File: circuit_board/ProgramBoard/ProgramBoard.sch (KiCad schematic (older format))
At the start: 3 parts, among them P1 CONN5X2, P2 TC2030_IDC, P3 TC2030_IDC

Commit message: examined the program board
try to switch to 10 pin tag cable to combine the programmer, UART, and power.
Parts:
- removed P2, P3: TC2030_IDC, SensorDemo_pcb:HEADER_3X2, symbol SensorDemo_connector:TC2030_IDC
- added P2: HEADER_6, SensorDemo_pcb:HEADER_6, symbol SensorDemo_connector:HEADER_6
- added U1: SparkFun_FT231X_Breakout, SensorDemo_pcb:SparkFun_FT231X_Breakout, symbol SensorDemo_discrete:SparkFun_FT231X_Breakout
- P1: value CONN5X2 -> IDC-10; footprint SensorDemo_pcb:FT231X_breakout -> SensorDemo_pcb:IDC_10
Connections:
- net labels removed: +5V, GND, PGC, PGD, PGM, RX, TX, VDD, VSS, ~MCLR
- wire segments 22 -> 0
- no-connect marks 6 -> 0
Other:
- note added: "IDC-10 connector"
- note added: "PICkit 3 connector"
- note removed: "From the USB, PIN 6 on top (in pic in ref)"
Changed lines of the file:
@@
 $EndDescr
 $Comp
-L SensorDemo_connector:TC2030_IDC P2
-U 1 1 6049E1C8
-P 2900 1700
-F 0 "P2" H 2900 1973 50  0000 C CNN
-F 1 "TC2030_IDC" H 2900 1250 50  0001 C CNN
-F 2 "SensorDemo_pcb:HEADER_3X2" H 6200 -450 60  0001 C CNN
-F 3 "" H 6200 -450 60  0000 C CNN
-	1    2900 1700
+L SensorDemo_discrete:SparkFun_FT231X_Breakout U1
+U 1 1 603DD946
+P 6800 3500
+F 0 "U1" H 6800 4187 60  0000 C CNN
+F 1 "SparkFun_FT231X_Breakout" H 6800 4081 60  0000 C CNN
+F 2 "SensorDemo_pcb:SparkFun_FT231X_Breakout" H 6800 3650 60  0001 C CNN
+F 3 "https://www.tag-connect.com/product/tc2050-idc-nl-10-pin-no-legs-cable-with-ribbon-connector" H 6800 3650 60  0001 C CNN
+	1    6800 3500
+	1    0    0    -1
+$EndComp
+Text Notes 6950 4650 0    50   ~ 0
+PICkit 3 connector
+$Comp
+L SensorDemo_connector:HEADER_6 P2
+U 1 1 603DF1C0
+P 7250 4800
+F 0 "P2" H 7588 4692 50  0000 L CNN
+F 1 "HEADER_6" H 7250 4250 50  0001 C CNN
+F 2 "SensorDemo_pcb:HEADER_6" H 10550 2600 60  0001 C CNN
+F 3 "" H 10550 2600 60  0000 C CNN
+	1    7250 4800
 	1    0    0    -1
 $EndComp
 $Comp
-L SensorDemo_connector:TC2030_IDC P3
-U 1 1 6049EA08
-P 2950 2800
-F 0 "P3" H 2950 3073 50  0000 C CNN
-F 1 "TC2030_IDC" H 2950 2350 50  0001 C CNN
-F 2 "SensorDemo_pcb:HEADER_3X2" H 6250 650 60  0001 C CNN
-F 3 "" H 6250 650 60  0000 C CNN
-	1    2950 2800
+L SensorDemo_connector:CONN5X2 P1
+U 1 1 603DFAE2
+P 5000 4850
+F 0 "P1" H 5000 5337 60  0000 C CNN
+F 1 "IDC-10" H 5000 5231 60  0000 C CNN
+F 2 "SensorDemo_pcb:IDC_10" H 8300 2700 60  0001 C CNN
+F 3 "" H 8300 2700 60  0000 C CNN
+	1    5000 4850
 	1    0    0    -1
 $EndComp
-Wire Wire Line
-	1900 1350 1900 1500
-Wire Wire Line
-	1900 1500 1800 1500
-$Comp
-L SensorDemo_power_supply:+5V #PS01
-U 1 1 604A19ED
-P 1900 1350
-F 0 "#PS01" H 1900 1300 50  0001 C CNN
-F 1 "+5V" H 1968 1378 50  0000 L CNN
-F 2 "" H 1905 1045 50  0001 C CNN
-F 3 "" H 1905 1045 50  0001 C CNN
-	1    1900 1350
-	1    0    0    -1
-$EndComp
-Wire Wire Line
-	2550 1800 2500 1800
-Wire Wire Line
-	2500 2000 3300 2000
-Wire Wire Line
-	3300 2000 3300 1800
-Wire Wire Line
-	3300 1800 3250 1800
-Wire Wire Line
-	2500 1800 2500 2000
-Wire Wire Line
-	2500 2050 2500 2000
-Connection ~ 2500 2000
-$Comp
-L SensorDemo_power_supply:+5V #PS03
-U 1 1 604A80D9
-P 2500 2050
-F 0 "#PS03" H 2500 2000 50  0001 C CNN
-F 1 "+5V" H 2432 2077 50  0000 R CNN
-F 2 "" H 2505 1745 50  0001 C CNN
-F 3 "" H 2505 1745 50  0001 C CNN
-	1    2500 2050
-	-1   0    0    1
-$EndComp
-Wire Wire Line
-	3250 1700 3300 1700
-Wire Wire Line
-	3300 1700 3300 1600
-Wire Wire Line
-	3300 1600 3250 1600
-Wire Wire Line
-	3300 1400 3300 1600
-Connection ~ 3300 1600
-$Comp
-L SensorDemo_power_supply:GND #PS04
-U 1 1 604A954E
-P 3300 1350
-F 0 "#PS04" H 3300 1225 50  0001 C CNN
-F 1 "GND" H 3300 1275 50  0001 C CNN
-F 2 "" H 3300 1350 50  0001 C CNN
-F 3 "" H 3300 1350 50  0001 C CNN
-	1    3300 1350
-	-1   0    0    1
-$EndComp
-Wire Wire Line
-	3550 2700 3300 2700
-Wire Wire Line
-	3550 2800 3300 2800
-Wire Wire Line
-	3550 2900 3300 2900
-Wire Wire Line
-	2350 2700 2600 2700
-Wire Wire Line
-	2350 2800 2600 2800
-Wire Wire Line
-	2350 2900 2600 2900
-Text Label 3550 2700 2    50   ~ 0
-~MCLR
-Text Label 3550 2800 2    50   ~ 0
-VSS
-Text Label 3550 2900 2    50   ~ 0
-PGC
-Text Label 2350 2700 0    50   ~ 0
-VDD
-Text Label 2350 2800 0    50   ~ 0
-PGD
-Text Label 2350 2900 0    50   ~ 0
-PGM
-Text Notes 1250 1100 0    50   ~ 0
-From the USB, PIN 6 on top (in pic in ref)
-$Comp
-L SensorDemo_connector:CONN5X2 P1
-U 1 1 604B47DD
-P 1450 1700
-F 0 "P1" H 1450 2187 60  0000 C CNN
-F 1 "CONN5X2" H 1450 2081 60  0000 C CNN
-F 2 "SensorDemo_pcb:FT231X_breakout" H 4750 -450 60  0000 C CNN
-F 3 "" H 4750 -450 60  0000 C CNN
-	1    1450 1700
-	1    0    0    -1
-$EndComp
-Wire Wire Line
-	900  1900 1100 1900
-Text Label 900  1900 0    50   ~ 0
-RX
-Wire Wire Line
-	2000 1900 1800 1900
-Text Label 2000 1900 2    50   ~ 0
-TX
-Wire Wire Line
-	1050 2050 1050 1500
-Wire Wire Line
-	1050 1500 1100 1500
-$Comp
-L SensorDemo_power_supply:GND #PS0101
-U 1 1 604BC56C
-P 1050 2100
-F 0 "#PS0101" H 1050 1975 50  0001 C CNN
-F 1 "GND" H 1050 2025 50  0001 C CNN
-F 2 "" H 1050 2100 50  0001 C CNN
-F 3 "" H 1050 2100 50  0001 C CNN
-	1    1050 2100
-	1    0    0    -1
-$EndComp
-NoConn ~ 1100 1600
-NoConn ~ 1100 1700
-NoConn ~ 1100 1800
-NoConn ~ 1800 1800
-NoConn ~ 1800 1700
-NoConn ~ 1800 1600
+Text Notes 4650 5350 0    50   ~ 0
+IDC-10 connector
 $EndSCHEMATC

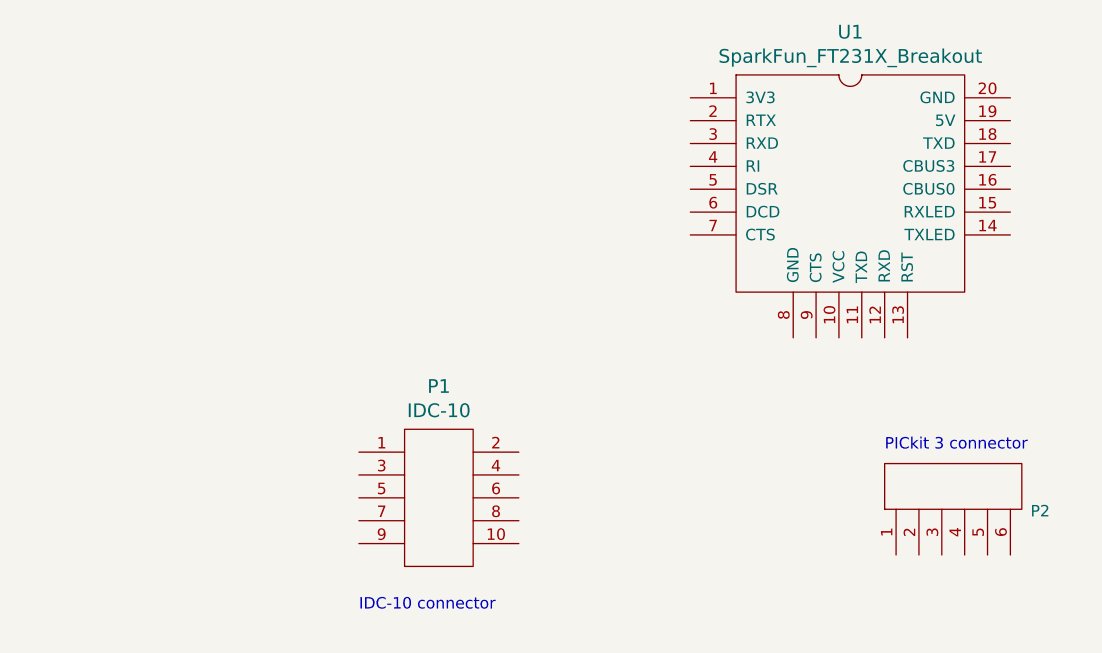
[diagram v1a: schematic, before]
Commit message: SensorDemo and Program board modified
1. SensorDemo board minor adjustment, 3D models added.
2. the TC2050 cable is added and routed on programmer board.
3. 3D models are added into the library.
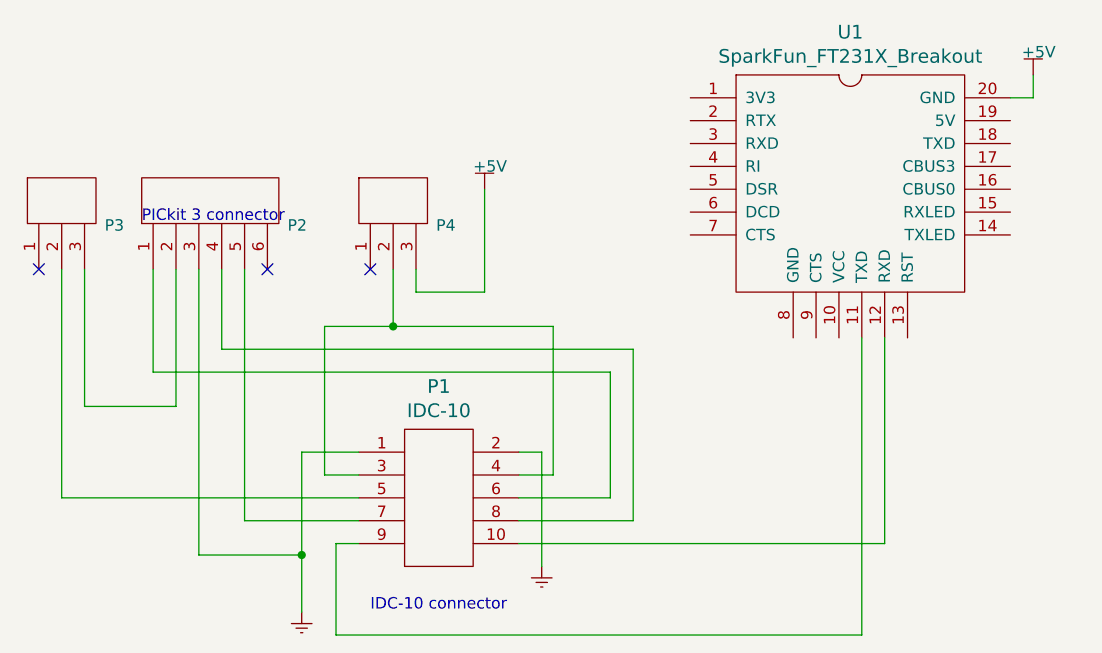
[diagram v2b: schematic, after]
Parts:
- added P3, P4: HEADER_3, SensorDemo_pcb:HEADER_3, symbol SensorDemo_connector:HEADER_3
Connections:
- net at U1.11 (TXD): now also P1.9
- net at U1.12 (RXD): now also P1.10
- net at P2.1: now also P1.6
- net at P2.2: now also P3.3
- net at P2.3: now also P1.1
- net at P2.4: now also P1.8
- net at P2.5: now also P1.7
- net at P1.3: now also P1.4, P4.2
- net at P1.5: now also P3.2
- no-connect marks 0 -> 3
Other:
- moved on the sheet: P2
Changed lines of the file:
@@
 	1    0    0    -1
 $EndComp
-Text Notes 6950 4650 0    50   ~ 0
+Text Notes 3700 3650 0    50   ~ 0
 PICkit 3 connector
 $Comp
 L SensorDemo_connector:HEADER_6 P2
 U 1 1 603DF1C0
-P 7250 4800
-F 0 "P2" H 7588 4692 50  0000 L CNN
-F 1 "HEADER_6" H 7250 4250 50  0001 C CNN
-F 2 "SensorDemo_pcb:HEADER_6" H 10550 2600 60  0001 C CNN
-F 3 "" H 10550 2600 60  0000 C CNN
-	1    7250 4800
+P 4000 3550
+F 0 "P2" H 4338 3442 50  0000 L CNN
+F 1 "HEADER_6" H 4000 3000 50  0001 C CNN
+F 2 "SensorDemo_pcb:HEADER_6" H 7300 1350 60  0001 C CNN
+F 3 "" H 7300 1350 60  0000 C CNN
+	1    4000 3550
 	1    0    0    -1
 $EndComp
@@
 	1    0    0    -1
 $EndComp
-Text Notes 4650 5350 0    50   ~ 0
+Text Notes 4700 5350 0    50   ~ 0
 IDC-10 connector
+$Comp
+L SensorDemo_power_supply:GND #PS03
+U 1 1 603D34E0
+P 5450 5200
+F 0 "#PS03" H 5450 5075 50  0001 C CNN
+F 1 "GND" H 5450 5125 50  0001 C CNN
+F 2 "" H 5450 5200 50  0001 C CNN
+F 3 "" H 5450 5200 50  0001 C CNN
+	1    5450 5200
+	1    0    0    -1
+$EndComp
+$Comp
+L SensorDemo_power_supply:+5V #PS01
+U 1 1 603D79A0
+P 7600 3000
+F 0 "#PS01" H 7600 2950 50  0001 C CNN
+F 1 "+5V" H 7550 3100 50  0000 L CNN
+F 2 "" H 7605 2695 50  0001 C CNN
+F 3 "" H 7605 2695 50  0001 C CNN
+	1    7600 3000
+	1    0    0    -1
+$EndComp
+Wire Wire Line
+	7600 3000 7600 3100
+Wire Wire Line
+	7600 3100 7500 3100
+Wire Wire Line
+	5350 4650 5450 4650
+Wire Wire Line
+	5450 4650 5450 5150
+Wire Wire Line
+	5350 4750 5500 4750
+Wire Wire Line
+	5500 4750 5500 4100
+Wire Wire Line
+	4500 4750 4500 4100
+Wire Wire Line
+	4500 4750 4650 4750
+Wire Wire Line
+	4650 4650 4400 4650
+Wire Wire Line
+	4400 4650 4400 5100
+$Comp
+L SensorDemo_power_supply:GND #PS04
+U 1 1 603DAB05
+P 4400 5400
+F 0 "#PS04" H 4400 5275 50  0001 C CNN
+F 1 "GND" H 4400 5325 50  0001 C CNN
+F 2 "" H 4400 5400 50  0001 C CNN
+F 3 "" H 4400 5400 50  0001 C CNN
+	1    4400 5400
+	1    0    0    -1
+$EndComp
+Wire Wire Line
+	3850 3850 3850 4450
+Wire Wire Line
+	3750 3850 3750 4300
+Wire Wire Line
+	3750 4300 5750 4300
+Wire Wire Line
+	5750 4300 5750 4850
+Wire Wire Line
+	5750 4850 5350 4850
+Wire Wire Line
+	3950 3850 3950 5100
+Wire Wire Line
+	3950 5100 4400 5100
+Connection ~ 4400 5100
+Wire Wire Line
+	4400 5100 4400 5350
+Wire Wire Line
+	4050 3850 4050 4200
+Wire Wire Line
+	4050 4200 5850 4200
+Wire Wire Line
+	5850 4200 5850 4950
+Wire Wire Line
+	5850 4950 5350 4950
+Wire Wire Line
+	4150 3850 4150 4950
+Wire Wire Line
+	4150 4950 4650 4950
+NoConn ~ 4250 3850
+Wire Wire Line
+	4650 5050 4550 5050
+Wire Wire Line
+	4550 5050 4550 5450
+Wire Wire Line
+	4550 5450 6850 5450
+Wire Wire Line
+	6850 5450 6850 4150
+Wire Wire Line
+	6950 4150 6950 5050
+Wire Wire Line
+	6950 5050 5350 5050
+Wire Wire Line
+	5500 4100 4800 4100
+$Comp
+L SensorDemo_connector:HEADER_3 P4
+U 1 1 603E9635
+P 4800 3550
+F 0 "P4" H 4988 3442 50  0000 L CNN
+F 1 "HEADER_3" H 4800 3000 50  0001 C CNN
+F 2 "SensorDemo_pcb:HEADER_3" H 8100 1350 60  0001 C CNN
+F 3 "" H 8100 1350 60  0000 C CNN
+	1    4800 3550
+	1    0    0    -1
+$EndComp
+$Comp
+L SensorDemo_power_supply:+5V #PS02
+U 1 1 603EB14F
+P 5200 3500
+F 0 "#PS02" H 5200 3450 50  0001 C CNN
+F 1 "+5V" H 5150 3600 50  0000 L CNN
+F 2 "" H 5205 3195 50  0001 C CNN
+F 3 "" H 5205 3195 50  0001 C CNN
+	1    5200 3500
+	1    0    0    -1
+$EndComp
+Wire Wire Line
+	5200 3500 5200 3950
+Wire Wire Line
+	4900 3850 4900 3950
+Wire Wire Line
+	4900 3950 5200 3950
+NoConn ~ 4700 3850
+Wire Wire Line
+	4800 3850 4800 4100
+Connection ~ 4800 4100
+Wire Wire Line
+	4800 4100 4500 4100
+$Comp
+L SensorDemo_connector:HEADER_3 P3
+U 1 1 603EEBCF
+P 3350 3550
+F 0 "P3" H 3538 3442 50  0000 L CNN
+F 1 "HEADER_3" H 3350 3000 50  0001 C CNN
+F 2 "SensorDemo_pcb:HEADER_3" H 6650 1350 60  0001 C CNN
+F 3 "" H 6650 1350 60  0000 C CNN
+	1    3350 3550
+	1    0    0    -1
+$EndComp
+Wire Wire Line
+	3450 3850 3450 4450
+NoConn ~ 3250 3850
+Wire Wire Line
+	3350 3850 3350 4850
+Wire Wire Line
+	3850 4450 3450 4450
+Wire Wire Line
+	4650 4850 3350 4850
 $EndSCHEMATC

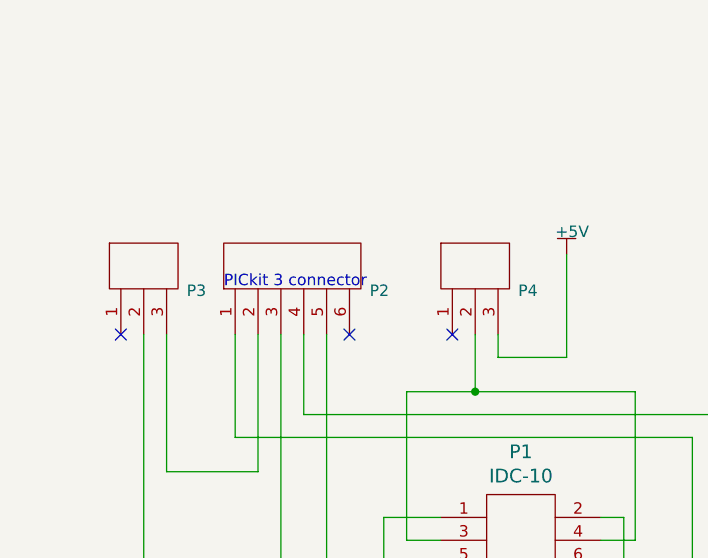
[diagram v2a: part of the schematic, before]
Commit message: updated SensoDemo and ProgramBoard
INA126 is replaced by INA333.
TC2050-IDC-NL cable will be used for powering and programming.
both boards should be done.
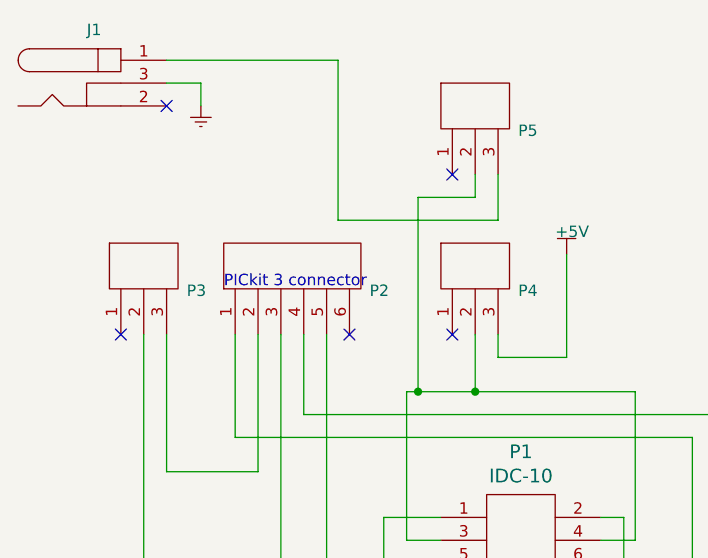
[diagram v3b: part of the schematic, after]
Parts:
- added J1: BARREL_JACK, SensorDemo_pcb:BARREL_JACK, symbol SensorDemo_connector:BARREL_JACK
- added P5: HEADER_3, SensorDemo_pcb:HEADER_3, symbol SensorDemo_connector:HEADER_3
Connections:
- net at P1.3, P1.4, P4.2: now also P5.2
- new net: J1.1, P5.3
- no-connect marks 3 -> 5
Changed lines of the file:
@@
 Connection ~ 4800 4100
 Wire Wire Line
-	4800 4100 4500 4100
+	4800 4100 4550 4100
 $Comp
 L SensorDemo_connector:HEADER_3 P3
@@
 Wire Wire Line
 	4650 4850 3350 4850
+$Comp
+L SensorDemo_connector:BARREL_JACK J1
+U 1 1 6047A3B5
+P 3150 2750
+F 0 "J1" H 3133 2983 50  0000 C CNN
+F 1 "BARREL_JACK" H 3150 2550 50  0001 C CNN
+F 2 "SensorDemo_pcb:BARREL_JACK" H 3150 2750 60  0001 C CNN
+F 3 "" H 3150 2750 60  0000 C CNN
+	1    3150 2750
+	1    0    0    -1
+$EndComp
+$Comp
+L SensorDemo_connector:HEADER_3 P5
+U 1 1 6047EE8D
+P 4800 2850
+F 0 "P5" H 4988 2742 50  0000 L CNN
+F 1 "HEADER_3" H 4800 2300 50  0001 C CNN
+F 2 "SensorDemo_pcb:HEADER_3" H 8100 650 60  0001 C CNN
+F 3 "" H 8100 650 60  0000 C CNN
+	1    4800 2850
+	1    0    0    -1
+$EndComp
+NoConn ~ 4700 3150
+Wire Wire Line
+	4800 3150 4800 3250
+Wire Wire Line
+	4800 3250 4550 3250
+Wire Wire Line
+	4550 3250 4550 4100
+Connection ~ 4550 4100
+Wire Wire Line
+	4550 4100 4500 4100
+Wire Wire Line
+	4900 3150 4900 3350
+Wire Wire Line
+	4900 3350 4200 3350
+Wire Wire Line
+	4200 3350 4200 2650
+Wire Wire Line
+	3450 2650 4200 2650
+$Comp
+L SensorDemo_power_supply:GND #PS?
+U 1 1 6048CCC2
+P 3600 2900
+F 0 "#PS?" H 3600 2775 50  0001 C CNN
+F 1 "GND" H 3600 2825 50  0001 C CNN
+F 2 "" H 3600 2900 50  0001 C CNN
+F 3 "" H 3600 2900 50  0001 C CNN
+	1    3600 2900
+	1    0    0    -1
+$EndComp
+Wire Wire Line
+	3600 2850 3600 2750
+Wire Wire Line
+	3600 2750 3450 2750
+NoConn ~ 3450 2850
 $EndSCHEMATC

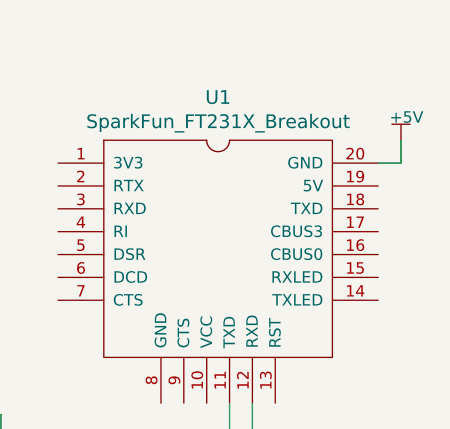
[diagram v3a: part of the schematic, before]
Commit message: updated schematic
-fixed programming board 5v
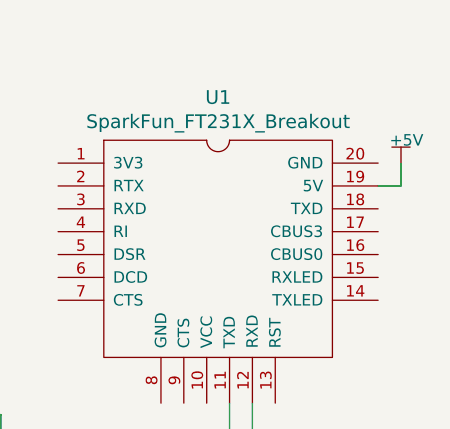
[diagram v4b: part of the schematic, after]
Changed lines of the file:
@@
 L SensorDemo_power_supply:+5V #PS01
 U 1 1 603D79A0
-P 7600 3000
-F 0 "#PS01" H 7600 2950 50  0001 C CNN
-F 1 "+5V" H 7550 3100 50  0000 L CNN
-F 2 "" H 7605 2695 50  0001 C CNN
-F 3 "" H 7605 2695 50  0001 C CNN
-	1    7600 3000
+P 7600 3100
+F 0 "#PS01" H 7600 3050 50  0001 C CNN
+F 1 "+5V" H 7550 3200 50  0000 L CNN
+F 2 "" H 7605 2795 50  0001 C CNN
+F 3 "" H 7605 2795 50  0001 C CNN
+	1    7600 3100
 	1    0    0    -1
 $EndComp
 Wire Wire Line
-	7600 3000 7600 3100
+	7600 3100 7600 3200
 Wire Wire Line
-	7600 3100 7500 3100
+	7600 3200 7500 3200
 Wire Wire Line
 	5350 4650 5450 4650

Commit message: Revert "Revert "Merge branch 'master' of https://github.com/zrs5532/mri_demo""
This reverts commit c7bcd66b67d9c03c78e75f611b5453059c538dec.
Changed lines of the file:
@@
 L SensorDemo_power_supply:+5V #PS01
 U 1 1 603D79A0
-P 7600 3100
-F 0 "#PS01" H 7600 3050 50  0001 C CNN
-F 1 "+5V" H 7550 3200 50  0000 L CNN
-F 2 "" H 7605 2795 50  0001 C CNN
-F 3 "" H 7605 2795 50  0001 C CNN
-	1    7600 3100
-	1    0    0    -1
-$EndComp
-Wire Wire Line
-	7600 3100 7600 3200
-Wire Wire Line
-	7600 3200 7500 3200
+P 7750 3100
+F 0 "#PS01" H 7750 3050 50  0001 C CNN
+F 1 "+5V" H 7700 3200 50  0000 L CNN
+F 2 "" H 7755 2795 50  0001 C CNN
+F 3 "" H 7755 2795 50  0001 C CNN
+	1    7750 3100
+	1    0    0    -1
+$EndComp
+Wire Wire Line
+	7750 3100 7750 3200
+Wire Wire Line
+	7750 3200 7500 3200
 Wire Wire Line
 	5350 4650 5450 4650
@@
 	4650 4850 3350 4850
 $Comp
+L SensorDemo_connector:HEADER_3 P5
+U 1 1 6047EE8D
+P 4800 2850
+F 0 "P5" H 4988 2742 50  0000 L CNN
+F 1 "HEADER_3" H 4800 2300 50  0001 C CNN
+F 2 "SensorDemo_pcb:HEADER_3" H 8100 650 60  0001 C CNN
+F 3 "" H 8100 650 60  0000 C CNN
+	1    4800 2850
+	1    0    0    -1
+$EndComp
+NoConn ~ 4700 3150
+Wire Wire Line
+	4800 3150 4800 3250
+Wire Wire Line
+	4800 3250 4550 3250
+Wire Wire Line
+	4550 3250 4550 4100
+Connection ~ 4550 4100
+Wire Wire Line
+	4550 4100 4500 4100
+Wire Wire Line
+	4900 3150 4900 3350
+Wire Wire Line
+	4900 3350 4200 3350
+Wire Wire Line
+	4200 3350 4200 2650
+$Comp
+L SensorDemo_power_supply:GND #PS0102
+U 1 1 6049968C
+P 6550 4350
+F 0 "#PS0102" H 6550 4225 50  0001 C CNN
+F 1 "GND" H 6550 4275 50  0001 C CNN
+F 2 "" H 6550 4350 50  0001 C CNN
+F 3 "" H 6550 4350 50  0001 C CNN
+	1    6550 4350
+	1    0    0    -1
+$EndComp
+Wire Wire Line
+	6550 4150 6550 4300
+$Comp
+L SensorDemo_power_supply:GND #PS0103
+U 1 1 604A6DE7
+P 7650 3500
+F 0 "#PS0103" H 7650 3375 50  0001 C CNN
+F 1 "GND" H 7650 3425 50  0001 C CNN
+F 2 "" H 7650 3500 50  0001 C CNN
+F 3 "" H 7650 3500 50  0001 C CNN
+	1    7650 3500
+	1    0    0    -1
+$EndComp
+Wire Wire Line
+	7650 3100 7650 3450
+Wire Wire Line
+	7650 3100 7500 3100
+NoConn ~ 3450 2750
+Wire Wire Line
+	3600 2850 3450 2850
+Wire Wire Line
+	3600 2950 3600 2850
+$Comp
+L SensorDemo_power_supply:GND #PS0101
+U 1 1 6048CCC2
+P 3600 3000
+F 0 "#PS0101" H 3600 2875 50  0001 C CNN
+F 1 "GND" H 3600 2925 50  0001 C CNN
+F 2 "" H 3600 3000 50  0001 C CNN
+F 3 "" H 3600 3000 50  0001 C CNN
+	1    3600 3000
+	1    0    0    -1
+$EndComp
+Wire Wire Line
+	3450 2650 4200 2650
+$Comp
 L SensorDemo_connector:BARREL_JACK J1
 U 1 1 6047A3B5
@@
 	1    0    0    -1
 $EndComp
-$Comp
-L SensorDemo_connector:HEADER_3 P5
-U 1 1 6047EE8D
-P 4800 2850
-F 0 "P5" H 4988 2742 50  0000 L CNN
-F 1 "HEADER_3" H 4800 2300 50  0001 C CNN
-F 2 "SensorDemo_pcb:HEADER_3" H 8100 650 60  0001 C CNN
-F 3 "" H 8100 650 60  0000 C CNN
-	1    4800 2850
-	1    0    0    -1
-$EndComp
-NoConn ~ 4700 3150
-Wire Wire Line
-	4800 3150 4800 3250
-Wire Wire Line
-	4800 3250 4550 3250
-Wire Wire Line
-	4550 3250 4550 4100
-Connection ~ 4550 4100
-Wire Wire Line
-	4550 4100 4500 4100
-Wire Wire Line
-	4900 3150 4900 3350
-Wire Wire Line
-	4900 3350 4200 3350
-Wire Wire Line
-	4200 3350 4200 2650
-Wire Wire Line
-	3450 2650 4200 2650
-$Comp
-L SensorDemo_power_supply:GND #PS?
-U 1 1 6048CCC2
-P 3600 2900
-F 0 "#PS?" H 3600 2775 50  0001 C CNN
-F 1 "GND" H 3600 2825 50  0001 C CNN
-F 2 "" H 3600 2900 50  0001 C CNN
-F 3 "" H 3600 2900 50  0001 C CNN
-	1    3600 2900
-	1    0    0    -1
-$EndComp
-Wire Wire Line
-	3600 2850 3600 2750
-Wire Wire Line
-	3600 2750 3450 2750
-NoConn ~ 3450 2850
 $EndSCHEMATC
